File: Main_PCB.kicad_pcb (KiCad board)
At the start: 4 copper layers, 161 x 70 mm, 69 parts, among them IC1 TCN75AVUA713-VAO, J1 Conn_Coaxial, J2 Conn_02x03_Odd_Even, J3 USB_C_Receptacle_USB2.0, J4 Conn_01x03_Male, J5 Conn_01x08, J6 Conn_01x08, SW1 SW_Push, SW2 SW_Push, U1 LTR-329ALS-01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

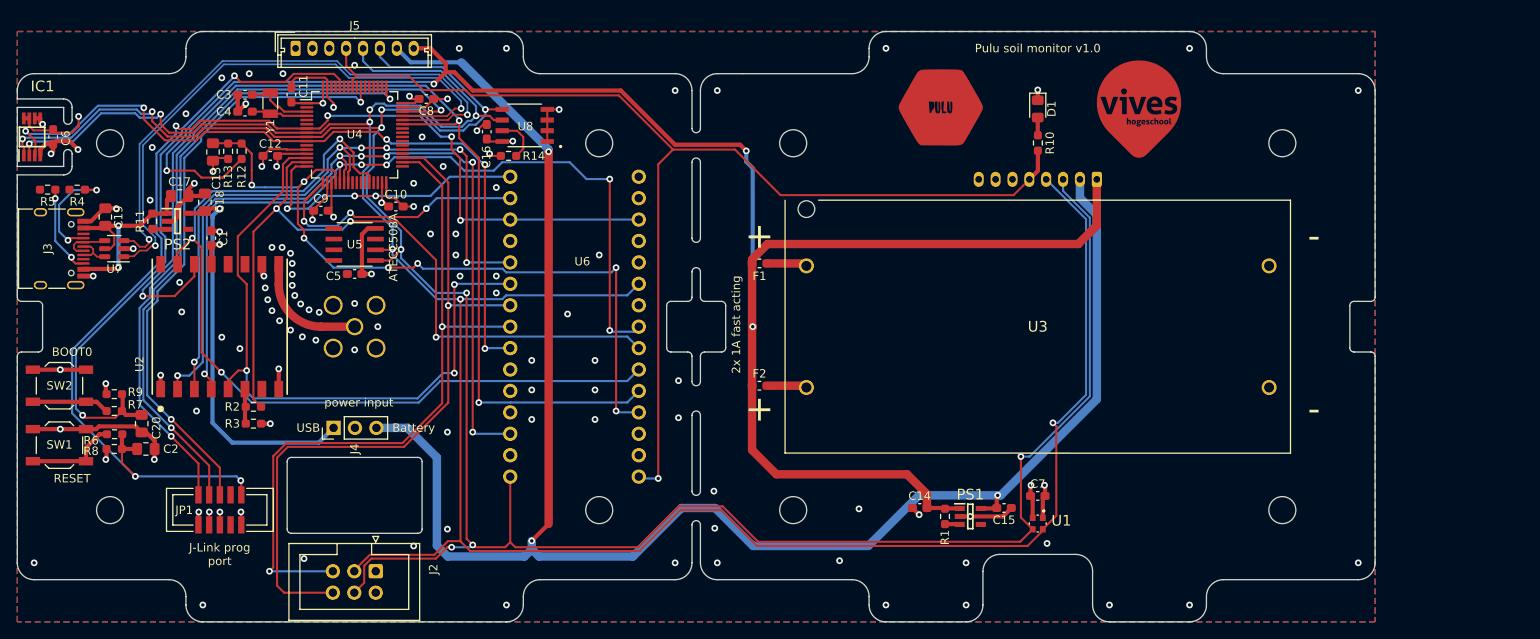
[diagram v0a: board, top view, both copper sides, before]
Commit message: separated pcb desgin into two
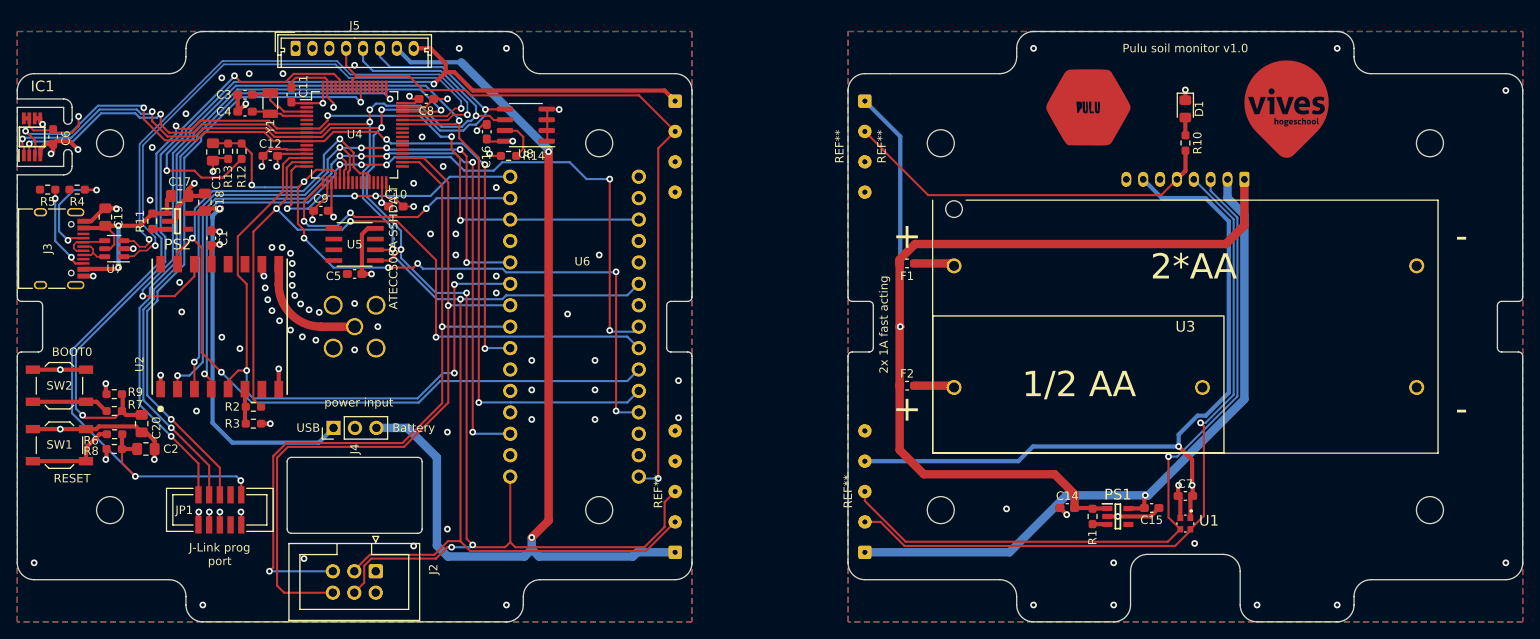
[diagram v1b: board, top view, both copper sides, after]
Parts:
- added REF**: SolderWire-0.1sqmm_1x05_P3.6mm_D0.4mm_OD1mm, Connector_Wire:SolderWire-0.1sqmm_1x05_P3.6mm_D0.4mm_OD1mm, F.Cu at (169.5, 124.8)
- added REF**: SolderWire-0.1sqmm_1x04_P3.6mm_D0.4mm_OD1mm, Connector_Wire:SolderWire-0.1sqmm_1x04_P3.6mm_D0.4mm_OD1mm, F.Cu at (147.0, 71.2)
- added REF**: SolderWire-0.1sqmm_1x05_P3.6mm_D0.4mm_OD1mm, Connector_Wire:SolderWire-0.1sqmm_1x05_P3.6mm_D0.4mm_OD1mm, F.Cu at (147.0, 124.8)
- added REF**: SolderWire-0.1sqmm_1x04_P3.6mm_D0.4mm_OD1mm, Connector_Wire:SolderWire-0.1sqmm_1x04_P3.6mm_D0.4mm_OD1mm, F.Cu at (169.5, 71.2)
- U5: value ATECC508A -> ATECC508A-SSHDA-T
- U8: footprint 24LC64-I_SN:SOIC127P599X175-8N -> Package_SO:SOIC-8_3.9x4.9mm_P1.27mm
- moved ? 17.5 mm to (178.5, 76.2)
- moved ? 17.5 mm to (196.0, 72.0)
- moved C14 17.5 mm to (193.5, 119.5)
- moved C15 17.5 mm to (203.5, 119.5)
- moved C7 17.5 mm to (207.5, 118.1)
- moved D1 17.5 mm to (207.5, 72.2)
- moved F1 17.5 mm to (174.5, 90.5)
- moved F2 17.5 mm to (174.5, 105.0)
- moved G*** 17.5 mm to (219.5, 73.0)
- moved J6 17.5 mm to (214.5, 80.5)
- moved PS1 17.5 mm to (199.5, 120.5)
- moved R1 17.5 mm to (196.5, 120.5)
- moved R10 17.5 mm to (207.5, 76.2)
- moved REF5 17.5 mm to (178.5, 76.2)
- moved REF6 17.5 mm to (178.5, 119.8)
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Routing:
- net VCC: track 56.5 -> 141.7 mm, vias 14 -> 15
- net /battery: track 211.6 -> 202.8 mm
- net /IC2_MoistureSensor_SCL1: track 299.3 -> 293.1 mm
- net VBAT: track 215.1 -> 211.6 mm, vias 4 -> 3
- net /LED: track 137.6 -> 134.9 mm
- net /IC2_MoistureSensor_SDA1: track 289.8 -> 288.6 mm
- net /bat_voltage: track 87.4 -> 86.7 mm
- net GND: vias 110 -> 103
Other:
- board size 161 x 70 mm -> 178.5 x 70 mm

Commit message: added battery 3d model and exported to blender for rendering
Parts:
- U8: value 24LC64-I/SN -> 24LC64-I_SN; footprint Package_SO:SOIC-8_3.9x4.9mm_P1.27mm -> Package_SO:SOP-8_3.9x4.9mm_P1.27mm
- moved U8 0.10 mm to (129.2, 74.1)
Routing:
- net VCC: track 141.7 -> 178.7 mm, vias 15 -> 16
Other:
- board text added: "3v3bat"
- board text added: "GND"
- board text added: "LED"
- board text added: "SCL"
- board text added: "SDA"
- board text added: "VBAT"
- board text added: "VCC"

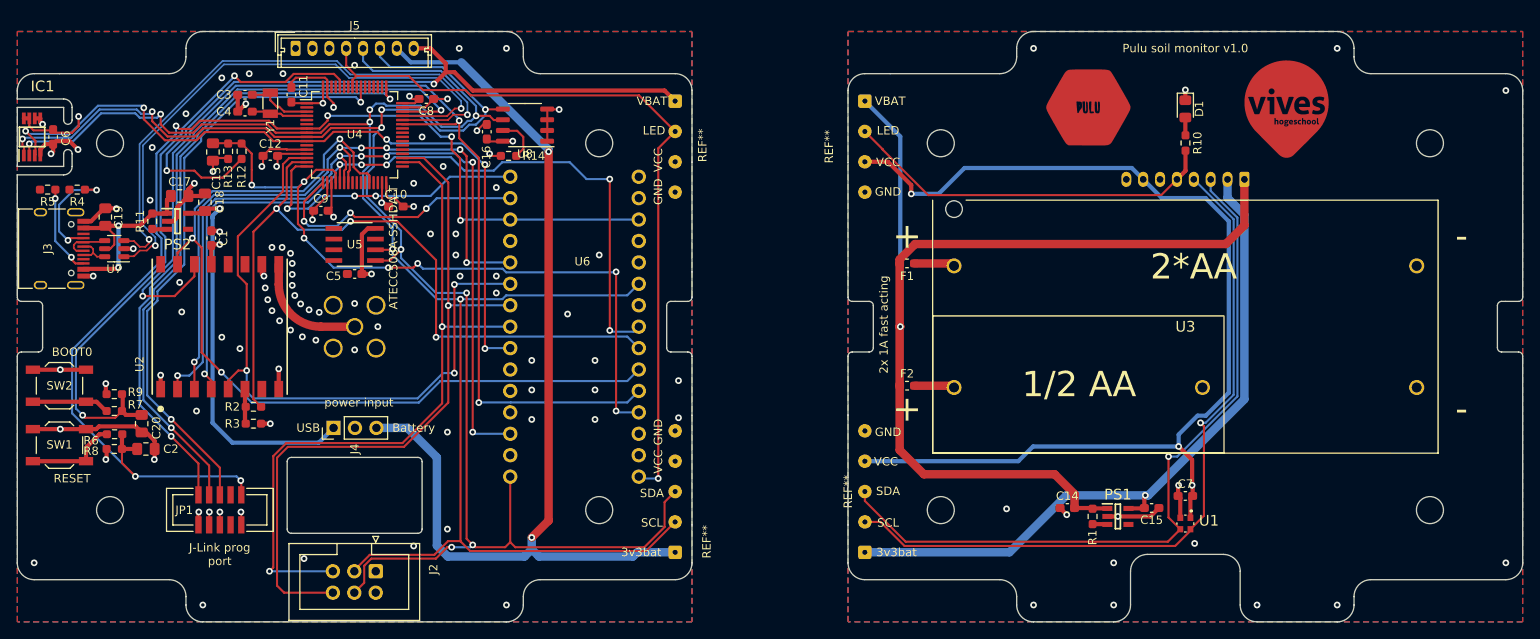
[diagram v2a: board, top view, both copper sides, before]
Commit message: made pcb order ready and ordered on jlcpcb
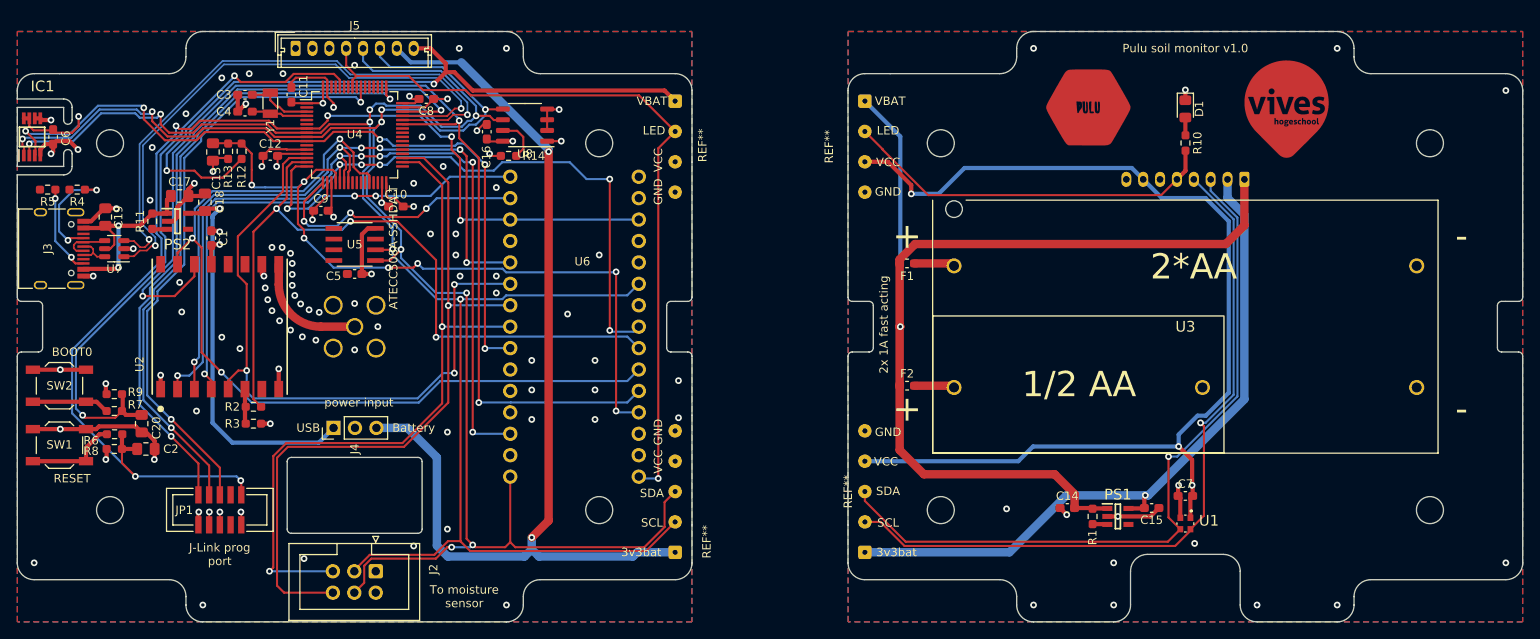
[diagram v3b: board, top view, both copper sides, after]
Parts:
- R3: value 4.7KR -> 100K
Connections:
- U8 pad 1: GND -> VCC
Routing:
- net VCC: track 178.7 -> 180.4 mm, vias 16 -> 17
- net GND: track 120.8 -> 120.1 mm
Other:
- board text added: "To moisture sensor"

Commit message: added general purpose button and updated layout
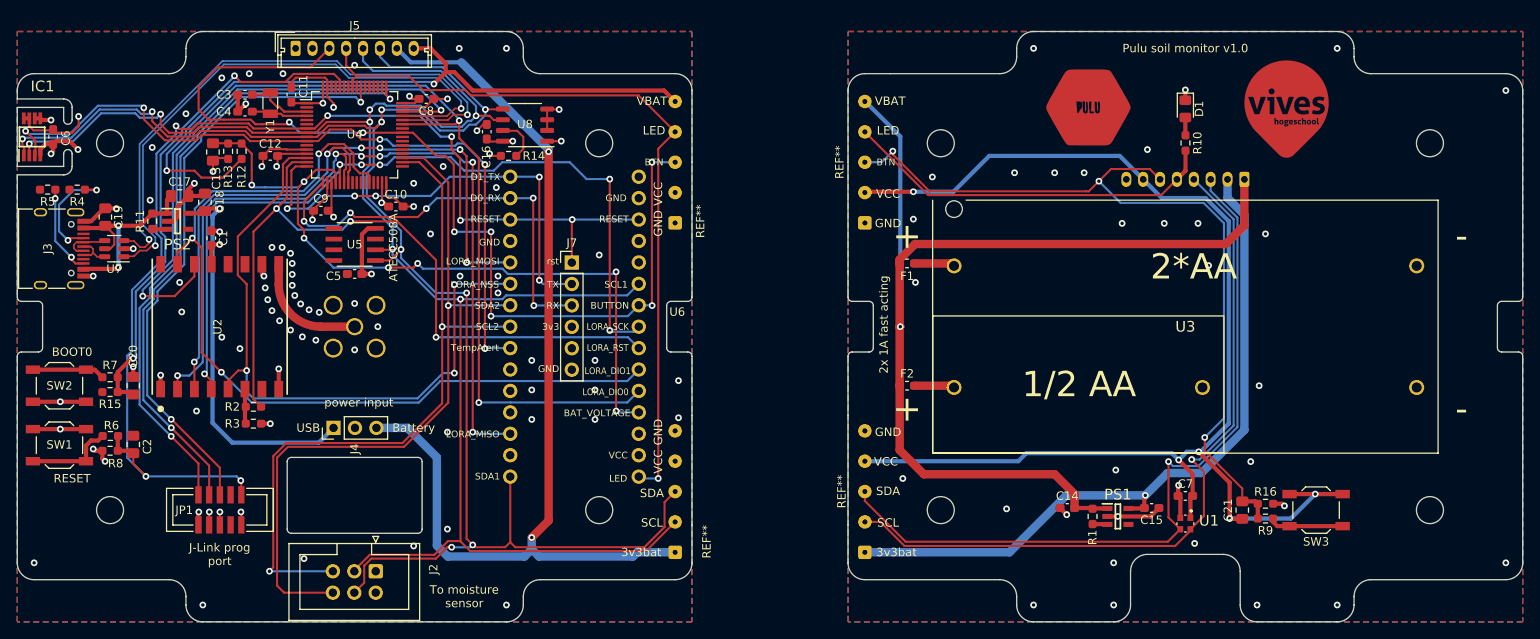
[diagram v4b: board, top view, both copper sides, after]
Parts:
- removed the REF** at (147.0, 71.2)
- removed the REF** at (169.5, 71.2)
- added C21: 100nF, Capacitor_SMD:C_0805_2012Metric_Pad1.18x1.45mm_HandSolder, F.Cu at (214.2, 119.8)
- added J7: Conn_01x06_Male, Connector_PinHeader_2.54mm:PinHeader_1x06_P2.54mm_Vertical, F.Cu at (134.8, 90.4)
- added R15: 100k, Resistor_SMD:R_0603_1608Metric_Pad0.98x0.95mm_HandSolder, F.Cu at (80.0, 105.8)
- added R16: 100k, Resistor_SMD:R_0603_1608Metric_Pad0.98x0.95mm_HandSolder, F.Cu at (217.0, 119.0)
- added REF**: SolderWire-0.1sqmm_1x05_P3.6mm_D0.4mm_OD1mm, Connector_Wire:SolderWire-0.1sqmm_1x05_P3.6mm_D0.4mm_OD1mm, F.Cu at (147.0, 85.7)
- added REF**: SolderWire-0.1sqmm_1x05_P3.6mm_D0.4mm_OD1mm, Connector_Wire:SolderWire-0.1sqmm_1x05_P3.6mm_D0.4mm_OD1mm, F.Cu at (169.5, 85.7)
- added SW3: SW_Push, Button_Switch_SMD:SW_SPST_TL3342, F.Cu at (223.0, 119.8)
- R9: value 100k -> 360R
- U5: value ATECC508A-SSHDA-T -> ATECC508A
- moved R9 137.3 mm to (217.0, 120.8), turned to 180 degrees
- moved C20 4.61 mm to (82.8, 105.0)
- moved R7 4.03 mm to (80.0, 104.0)
- moved C2 1.59 mm to (82.8, 112.0), turned to 90 degrees
- moved R6 0.54 mm to (80.0, 111.0)
- moved R8 0.54 mm to (80.0, 112.7)
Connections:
- net /D0_TX renamed /D0_RX
- C20 pad 1: /boot0 -> VCC
- C20 pad 2: GND -> /boot0
- J5 pad 3: unconnected-(J5-Pad3) -> /button
- J6 pad 6: unconnected-(J6-Pad6) -> /button
- R9 pad 1: VCC -> Net-(R9-Pad1)
- R9 pad 2: /boot0 -> /button
- SW2 pad 1: GND -> Net-(R7-Pad1)
- SW2 pad 2: Net-(R7-Pad1) -> VCC
- U4 pad 41: unconnected-(U4-Pad41) -> /button
- U6 pad 24: unconnected-(U6-Pad24) -> /button
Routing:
- net /button: track 0.00 -> 210.8 mm, vias 0 -> 10
- net VCC: track 180.4 -> 215.8 mm, vias 17 -> 21
- net /D0_RX: track 32.0 -> 52.0 mm, vias 3 -> 5
- net /D1_TX: track 34.8 -> 54.5 mm, vias 3 -> 5
- net GND: track 120.1 -> 104.1 mm, vias 103 -> 114
- net /boot0: track 72.8 -> 60.1 mm
- net Net-(R9-Pad1): track 0.00 -> 8.85 mm
- net /IC2_MoistureSensor_SDA1: track 288.9 -> 291.0 mm
- net /battery: track 202.8 -> 205.0 mm
- net /SPI_LORA_MOSI: track 80.3 -> 82.4 mm
- net /Reset: track 139.3 -> 137.3 mm, vias 6 -> 7
- net /SPI_LORA_MISO: track 99.2 -> 100.7 mm
- net /IC2_MoistureSensor_SCL1: track 293.1 -> 293.9 mm
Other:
- board text added: "3v3"
- board text added: "BAT_VOLTAGE"
- board text added: "BTN"
- board text added: "BUTTON"
- board text added: "D0_RX"
- board text added: "D1_TX"
- board text added: "LORA_DIO0"
- board text added: "LORA_DIO1"
- board text added: "LORA_MISO"
- board text added: "LORA_MOSI"
- board text added: "LORA_NSS"
- board text added: "LORA_RST"
- board text added: "LORA_SCK"
- board text added: "RX"
- board text added: "SCL1"
- board text added: "SCL2"
- board text added: "SDA1"
- board text added: "SDA2"
- board text added: "TX"
- board text added: "TempAlert"
- board text added: "rst"
